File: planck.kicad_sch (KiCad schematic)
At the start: 131 parts, among them J1 USB_C_U262-161N-4BVC11, J2 USB_C_U262-161N-4BVC11, J3 USB_C_U262-161N-4BVC11, SW1 SW_Hotswap_Kailh_Choc_V1_1u, SW10 SW_Hotswap_Kailh_Choc_V1_1u, SW11 SW_Hotswap_Kailh_Choc_V1_1u, SW12 SW_Hotswap_Kailh_Choc_V1_1u, SW13 SW_Hotswap_Kailh_Choc_V1_1u, SW14 SW_Hotswap_Kailh_Choc_V1_1u, SW15 SW_Hotswap_Kailh_Choc_V1_1u, SW16 SW_Hotswap_Kailh_Choc_V1_1u, SW17 SW_Hotswap_Kailh_Choc_V1_1u, SW18 SW_Hotswap_Kailh_Choc_V1_1u, SW19 SW_Hotswap_Kailh_Choc_V1_1u, SW2 SW_Hotswap_Kailh_Choc_V1_1u, SW20 SW_Hotswap_Kailh_Choc_V1_1u, SW21 SW_Hotswap_Kailh_Choc_V1_1u, SW22 SW_Hotswap_Kailh_Choc_V1_1u, SW23 SW_Hotswap_Kailh_Choc_V1_1u, SW24 SW_Hotswap_Kailh_Choc_V1_1u, SW25 SW_Push, SW3 SW_Hotswap_Kailh_Choc_V1_1u, SW4 SW_Hotswap_Kailh_Choc_V1_1u, SW5 SW_Hotswap_Kailh_Choc_V1_1u, SW6 SW_Hotswap_Kailh_Choc_V1_1u, SW7 SW_Hotswap_Kailh_Choc_V1_1u, SW8 SW_Hotswap_Kailh_Choc_V1_1u, SW9 SW_Hotswap_Kailh_Choc_V1_1u, U1 RP2040 ARM Cortex-M0 133MHz, U2 ME6219C33M5G, U3 W25Q16JVUXIQ, Y1 32MHz ±10ppm 20pF SMD3225-4P

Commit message: almost done
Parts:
- H1, H2, H3, H4: footprint MountingHole:MountingHole_2.7mm_M2.5 -> MountingHole:MountingHole_2.2mm_M2
- SW25: footprint (none) -> Switches:B3U-1000P; JLC (none) -> C231329
- U3: MANUFACTURER Winbond Electronics Corp. -> (none)
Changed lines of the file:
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@@
       (effects (font (size 1.27 1.27)) (justify left))
     )
-    (property "Footprint" "MountingHole:MountingHole_2.7mm_M2.5" (at 185.3522 155.9386 0)
+    (property "Footprint" "MountingHole:MountingHole_2.2mm_M2" (at 185.3522 155.9386 0)
       (effects (font (size 1.27 1.27)) hide)
     )
@@
       (effects (font (size 1.27 1.27)) (justify left))
     )
-    (property "Footprint" "MountingHole:MountingHole_2.7mm_M2.5" (at 185.3522 166.0986 0)
+    (property "Footprint" "MountingHole:MountingHole_2.2mm_M2" (at 185.3522 166.0986 0)
       (effects (font (size 1.27 1.27)) hide)
     )
@@
     )
     (property "Datasheet" "" (at 254 143.51 0)
-      (effects (font (size 1.27 1.27)) hide)
-    )
-    (property "LCSC" "" (at 254 143.51 0)
       (effects (font (size 1.27 1.27)) hide)
     )
@@
       (effects (font (size 1.27 1.27)) (justify left bottom) hide)
     )
-    (property "MANUFACTURER" "Winbond Electronics Corp." (at 358.14 44.45 0)
-      (effects (font (size 1.27 1.27)) (justify left bottom) hide)
-    )
     (property "JLC" "C2843335" (at 358.14 44.45 0)
       (effects (font (size 1.27 1.27)) hide)
@@
       (effects (font (size 1.27 1.27)) (justify left))
     )
-    (property "Footprint" "MountingHole:MountingHole_2.7mm_M2.5" (at 185.42 161.29 0)
+    (property "Footprint" "MountingHole:MountingHole_2.2mm_M2" (at 185.42 161.29 0)
       (effects (font (size 1.27 1.27)) hide)
     )
@@
       (effects (font (size 1.27 1.27)))
     )
-    (property "Footprint" "" (at 309.88 31.75 0)
+    (property "Footprint" "Switches:B3U-1000P" (at 309.88 31.75 0)
       (effects (font (size 1.27 1.27)) hide)
     )
     (property "Datasheet" "~" (at 309.88 31.75 0)
+      (effects (font (size 1.27 1.27)) hide)
+    )
+    (property "JLC" "C231329" (at 309.88 36.83 0)
       (effects (font (size 1.27 1.27)) hide)
     )
@@
       (effects (font (size 1.27 1.27)) (justify left))
     )
-    (property "Footprint" "MountingHole:MountingHole_2.7mm_M2.5" (at 185.3522 171.1786 0)
-      (effects (font (size 1.27 1.27)) hide)
-    )
+    (property "Footprint" "MountingHole:MountingHole_2.2mm_M2" (at 185.3522 171.1786 0)
+      (effects (font (size 1.27 1.27)) hide)
+    )

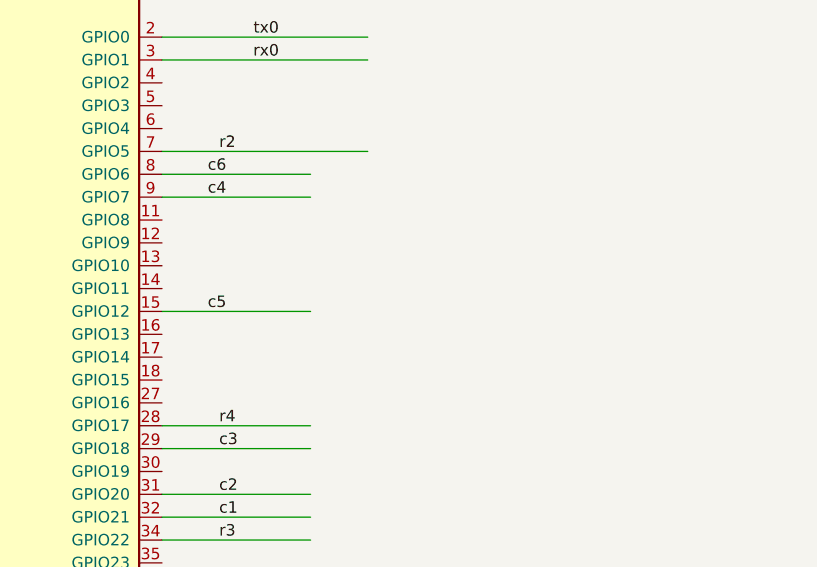
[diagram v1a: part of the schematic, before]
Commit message: ADD SWITCH HANDSET
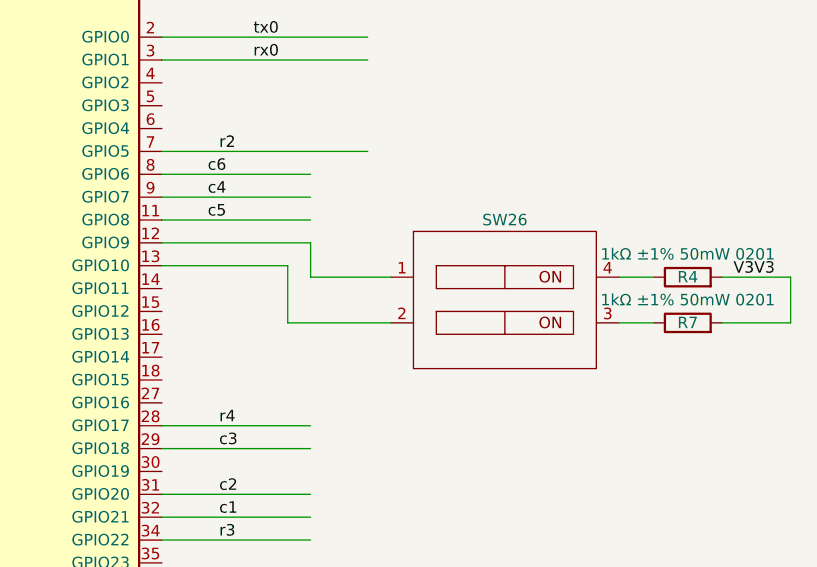
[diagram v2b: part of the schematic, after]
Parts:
- added R4, R7: 1kΩ ±1% 50mW 0201, Resistor_SMD:R_0201_0603Metric, symbol Device:R
- added SW26: ~, Switches:DSHP02TSGET, symbol MCU_RaspberryPi_and_Boards:DSHP02TSGET
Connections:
- net V3V3: now also R4.2, R7.2
- net c5: now also U1.11 (GPIO8); no longer U1.15 (GPIO12)
- net at U1.12 (GPIO9): now also SW26.1
- net at U1.13 (GPIO10): now also SW26.2
- new net: R7.1, SW26.3
- new net: R4.1, SW26.4
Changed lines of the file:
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@@
     (stroke (width 0) (type default))
   )
+  (wire (pts (xy 337.82 187.96) (xy 337.82 194.31))
+    (stroke (width 0) (type default))
+  )
   (wire (pts (xy 118.11 101.6) (xy 118.11 125.73))
     (stroke (width 0) (type default))
@@
     (stroke (width 0) (type default))
   )
+  (wire (pts (xy 374.65 189.23) (xy 378.46 189.23))
+    (stroke (width 0) (type default))
+  )
   (wire (pts (xy 64.77 151.13) (xy 87.63 151.13))
     (stroke (width 0) (type default))
@@
     (stroke (width 0) (type default))
   )
+  (wire (pts (xy 393.7 189.23) (xy 393.7 194.31))
+    (stroke (width 0) (type default))
+  )
   (wire (pts (xy 308.61 113.03) (xy 316.23 113.03))
     (stroke (width 0) (type default))
@@
     (stroke (width 0) (type default))
   )
+  (wire (pts (xy 337.82 194.31) (xy 349.25 194.31))
+    (stroke (width 0) (type default))
+  )
   (wire (pts (xy 323.85 205.74) (xy 340.36 205.74))
     (stroke (width 0) (type default))
@@
     (stroke (width 0) (type default))
   )
+  (wire (pts (xy 340.36 189.23) (xy 349.25 189.23))
+    (stroke (width 0) (type default))
+  )
   (wire (pts (xy 71.12 207.01) (xy 78.74 207.01))
     (stroke (width 0) (type default))
@@
     (stroke (width 0) (type default))
   )
+  (wire (pts (xy 323.85 185.42) (xy 340.36 185.42))
+    (stroke (width 0) (type default))
+  )
   (wire (pts (xy 337.82 87.63) (xy 337.82 85.09))
     (stroke (width 0) (type default))
@@
     (stroke (width 0) (type default))
   )
-  (wire (pts (xy 323.85 193.04) (xy 340.36 193.04))
+  (wire (pts (xy 323.85 182.88) (xy 340.36 182.88))
     (stroke (width 0) (type default))
   )
@@
     (stroke (width 0) (type default))
   )
+  (wire (pts (xy 340.36 185.42) (xy 340.36 189.23))
+    (stroke (width 0) (type default))
+  )
   (wire (pts (xy 93.98 207.01) (xy 99.06 207.01))
     (stroke (width 0) (type default))
@@
     (stroke (width 0) (type default))
   )
+  (wire (pts (xy 386.08 194.31) (xy 393.7 194.31))
+    (stroke (width 0) (type default))
+  )
   (wire (pts (xy 121.92 91.44) (xy 124.46 91.44))
     (stroke (width 0) (type default))
@@
     (stroke (width 0) (type default))
   )
+  (wire (pts (xy 374.65 194.31) (xy 378.46 194.31))
+    (stroke (width 0) (type default))
+  )
   (wire (pts (xy 140.97 270.51) (xy 148.59 270.51))
     (stroke (width 0) (type default))
@@
     (stroke (width 0) (type default))
   )
+  (wire (pts (xy 386.08 189.23) (xy 393.7 189.23))
+    (stroke (width 0) (type default))
+  )
   (wire (pts (xy 31.75 171.45) (xy 31.75 182.88))
     (stroke (width 0) (type default))
@@
     (stroke (width 0) (type default))
   )
+  (wire (pts (xy 323.85 187.96) (xy 337.82 187.96))
+    (stroke (width 0) (type default))
+  )
   (wire (pts (xy 132.08 173.99) (xy 154.94 173.99))
     (stroke (width 0) (type default))
@@
     (effects (font (size 1.27 1.27)) (justify left bottom))
   )
+  (label "V3V3" (at 387.35 189.23 0) (fields_autoplaced)
+    (effects (font (size 1.27 1.27)) (justify left bottom))
+  )
   (label "VBUS" (at 77.47 173.99 0) (fields_autoplaced)
     (effects (font (size 1.27 1.27)) (justify left bottom))
@@
     (effects (font (size 1.27 1.27)) (justify left bottom))
   )
-  (label "c5" (at 328.93 193.04 0) (fields_autoplaced)
+  (label "c5" (at 328.93 182.88 0) (fields_autoplaced)
     (effects (font (size 1.27 1.27)) (justify left bottom))
   )
@@
     )
   )
+  (symbol (lib_id "Device:R") (at 382.27 194.31 90) (unit 1)
+    (in_bom yes) (on_board yes) (dnp no)
+    (property "Reference" "R7" (at 382.27 194.31 90)
+      (effects (font (size 1.27 1.27)))
+    )
+    (property "Value" "1kΩ ±1% 50mW 0201" (at 382.27 191.77 90)
+      (effects (font (size 1.27 1.27)))
+    )
+    (property "Footprint" "Resistor_SMD:R_0201_0603Metric" (at 382.27 196.088 90)
+      (effects (font (size 1.27 1.27)) hide)
+    )
+    (property "Datasheet" "https://atta.szlcsc.com/upload/public/pdf/source/20171107/C138165_15100517338981097059.pdf" (at 382.27 194.31 0)
+      (effects (font (size 1.27 1.27)) hide)
+    )
+    (property "JLC" "C138165" (at 382.27 194.31 90)
+      (effects (font (size 1.27 1.27)) hide)
+    )
+    (pin "1")
+    (pin "2")
+    (instances
+      (project "planck"
+        (path "/27312bda-a56e-4031-ad08-90fe6bbef090"
+          (reference "R7") (unit 1)
+        )
+      )
+    )
+  )
   (symbol (lib_id "Diode:1N4148W") (at 158.75 73.66 180) (unit 1)
     (in_bom yes) (on_board yes) (dnp no)
@@
     )
   )
+  (symbol (lib_id "MCU_RaspberryPi_and_Boards:DSHP02TSGET") (at 361.95 191.77 0) (unit 1)
+    (in_bom yes) (on_board yes) (dnp no) (fields_autoplaced)
+    (property "Reference" "SW26" (at 361.95 182.88 0)
+      (effects (font (size 1.27 1.27)))
+    )
+    (property "Value" "~" (at 361.95 191.77 0)
+      (effects (font (size 1.27 1.27)))
+    )
+    (property "Footprint" "Switches:DSHP02TSGET" (at 361.95 191.77 0)
+      (effects (font (size 1.27 1.27)) hide)
+    )
+    (property "Datasheet" "" (at 361.95 191.77 0)
+      (effects (font (size 1.27 1.27)) hide)
+    )
+    (property "JLC" "C40735" (at 361.95 191.77 0)
+      (effects (font (size 1.27 1.27)) hide)
+    )
+    (pin "1")
+    (pin "2")
+    (pin "3")
+    (pin "4")
+    (instances
+      (project "planck"
+        (path "/27312bda-a56e-4031-ad08-90fe6bbef090"
+          (reference "SW26") (unit 1)
+        )
+      )
+    )
+  )
   (symbol (lib_id "power:GND") (at 222.25 73.66 0) (unit 1)
     (in_bom yes) (on_board yes) (dnp no) (fields_autoplaced)
@@
         )
       )
+    )
+  )
+  (symbol (lib_id "Device:R") (at 382.27 189.23 90) (unit 1)
+    (in_bom yes) (on_board yes) (dnp no)
+    (property "Reference" "R4" (at 382.27 189.23 90)
+      (effects (font (size 1.27 1.27)))
+    )
+    (property "Value" "1kΩ ±1% 50mW 0201" (at 382.27 186.69 90)
+      (effects (font (size 1.27 1.27)))
+    )
+    (property "Footprint" "Resistor_SMD:R_0201_0603Metric" (at 382.27 191.008 90)
+      (effects (font (size 1.27 1.27)) hide)
+    )
+    (property "Datasheet" "https://atta.szlcsc.com/upload/public/pdf/source/20171107/C138165_15100517338981097059.pdf" (at 382.27 189.23 0)
+      (effects (font (size 1.27 1.27)) hide)
+    )
+    (property "JLC" "C138165" (at 382.27 189.23 90)
+      (effects (font (size 1.27 1.27)) hide)
+    )
+    (pin "1")
+    (pin "2")
+    (instances
+      (project "planck"
+        (path "/27312bda-a56e-4031-ad08-90fe6bbef090"
+          (reference "R4") (unit 1)
+        )
+      )

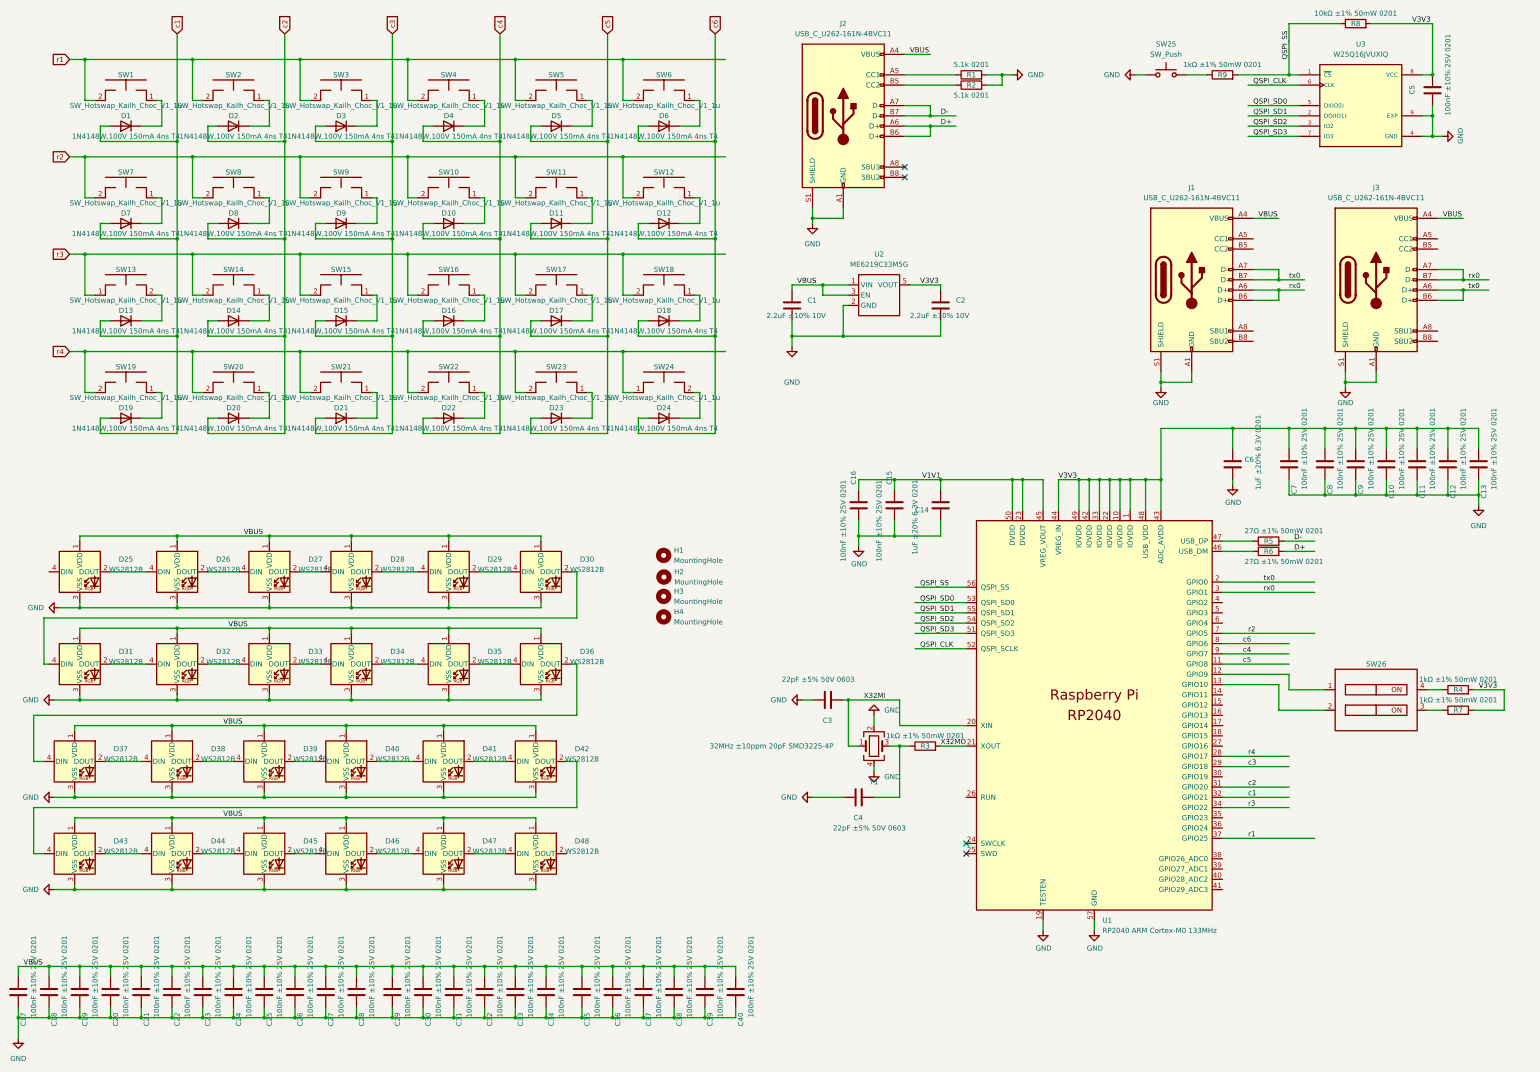
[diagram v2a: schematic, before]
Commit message: connect LED, add case
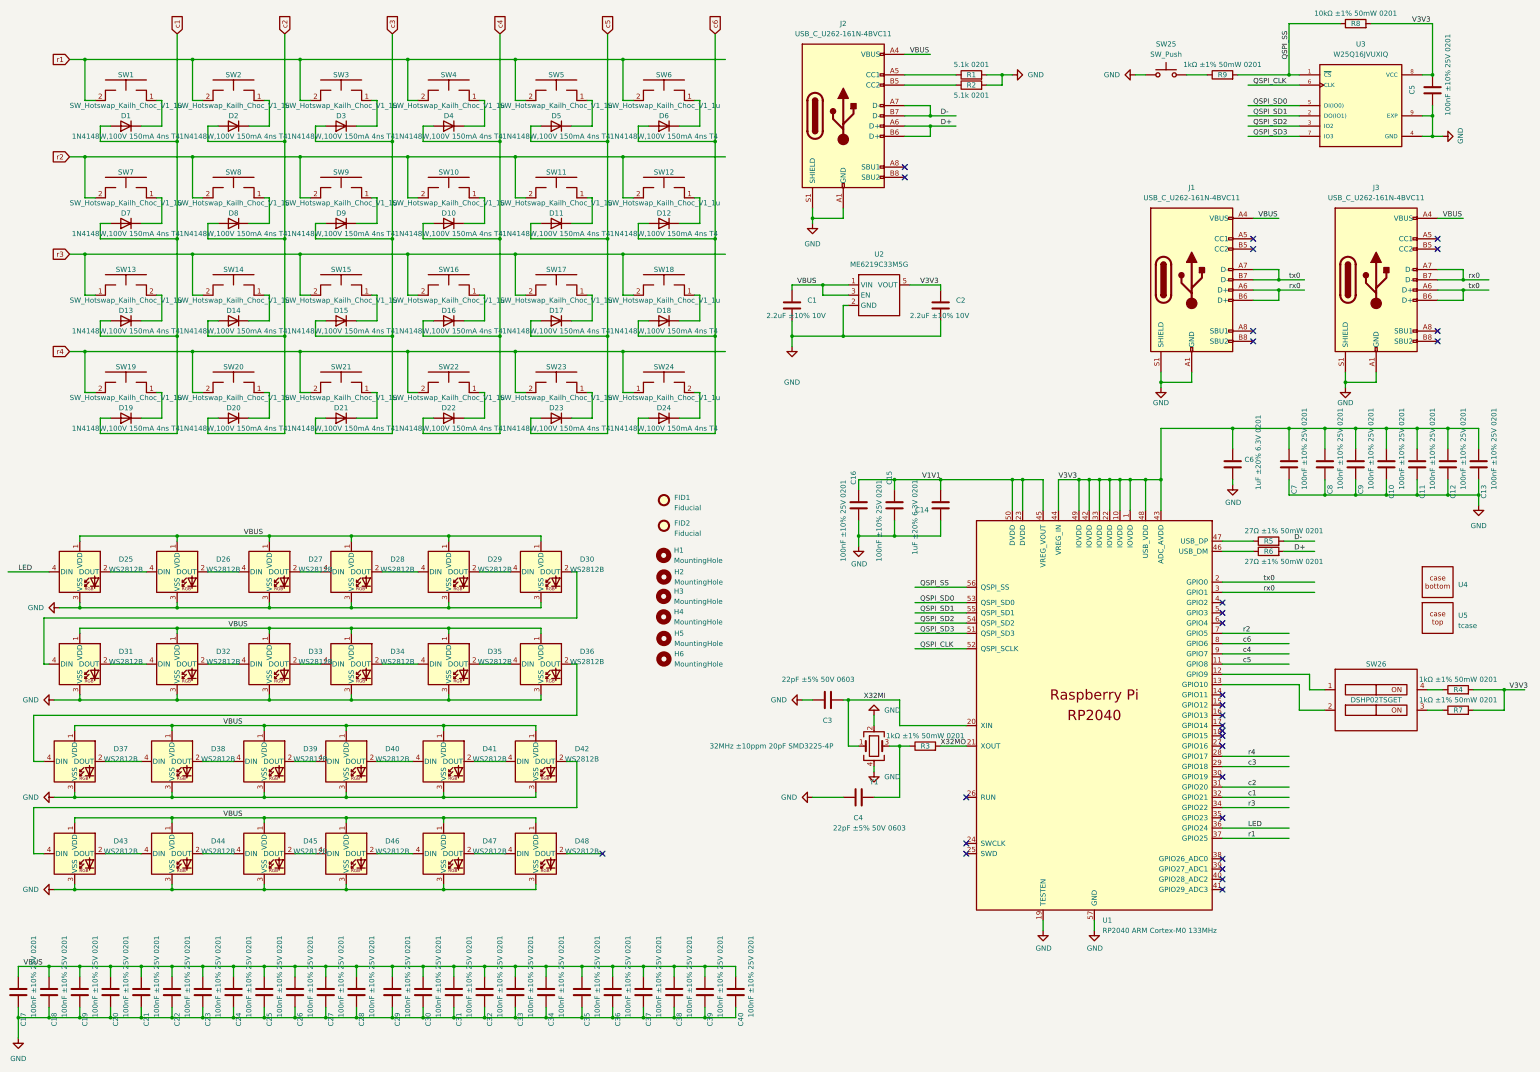
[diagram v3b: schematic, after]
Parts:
- added FID1, FID2: Fiducial, Fiducial:Fiducial_0.5mm_Mask1.5mm, symbol Mechanical:Fiducial
- added H5, H6: MountingHole, MountingHole:MountingHole_2.2mm_M2, symbol Mechanical:MountingHole
- added U4: ~, MCU_RaspberryPi_and_Boards:bcase, symbol MCU_RaspberryPi_and_Boards:bcase
- added U5: tcase, MCU_RaspberryPi_and_Boards:tcase, symbol MCU_RaspberryPi_and_Boards:tcase
- SW26: value ~ -> DSHP02TSGET
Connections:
- net LED: now reaches U1.36 (GPIO24)
- net LED: now also D25.4 (DIN)
- no-connect marks 4 -> 30
